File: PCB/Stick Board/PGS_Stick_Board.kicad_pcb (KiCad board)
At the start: 2 copper layers, 37.5 x 29.7 mm, 10 parts, among them J1 Molex 505110-0892, SW1 GL1807SYAE-002

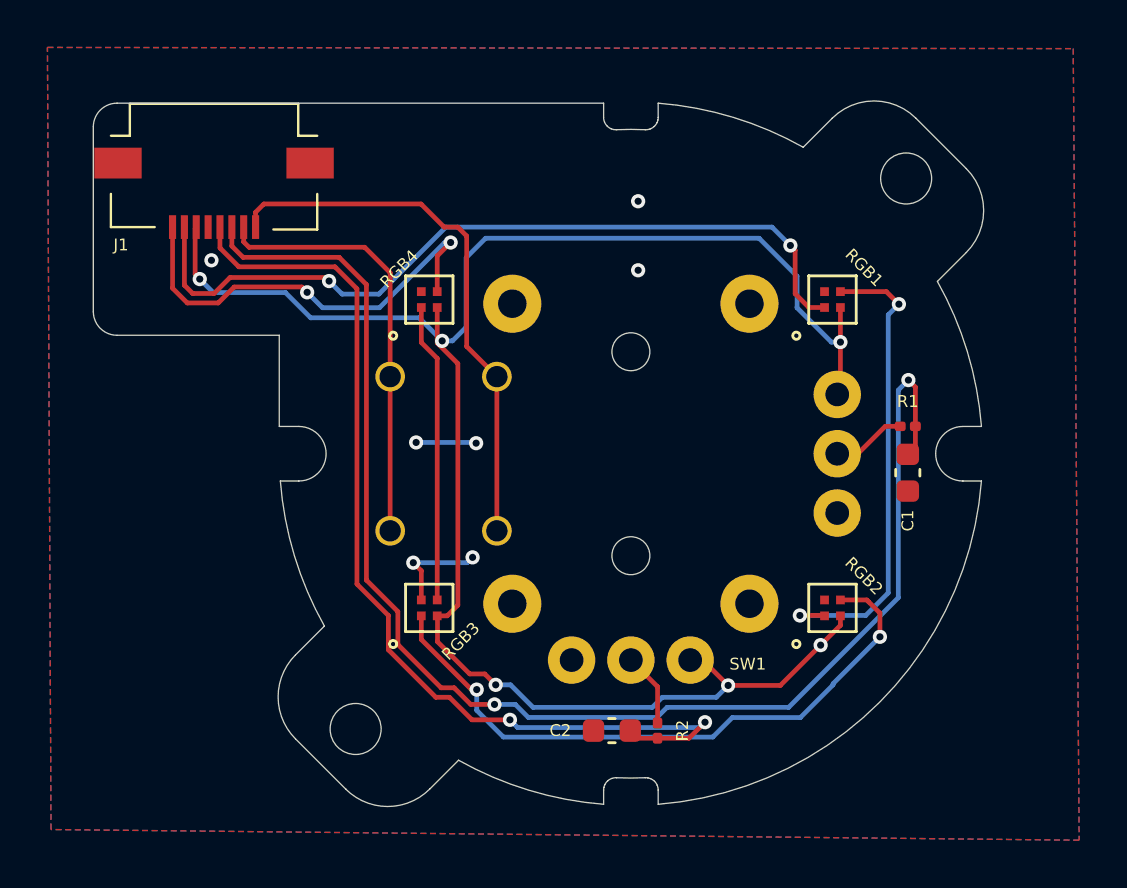
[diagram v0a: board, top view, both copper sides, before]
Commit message: Final Routing 3D Export
- Export 3D STEP models
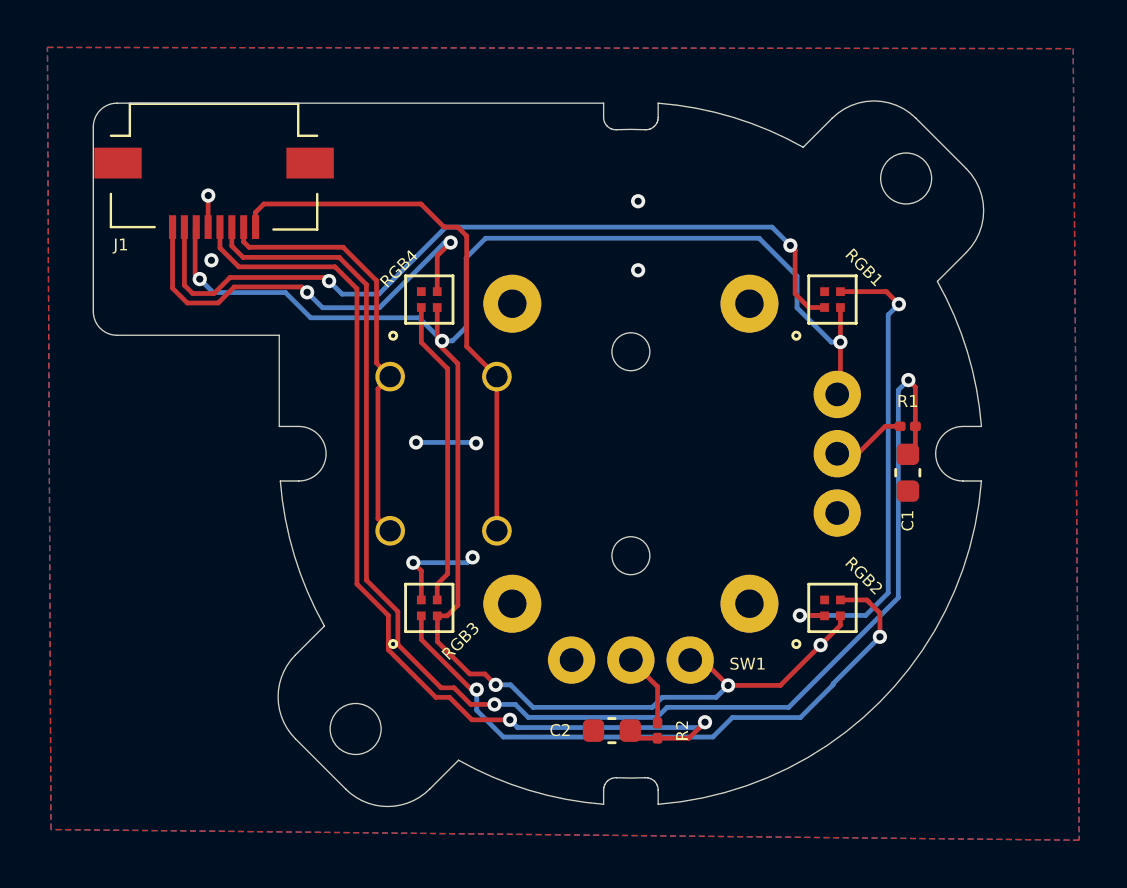
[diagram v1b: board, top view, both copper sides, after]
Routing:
- net GND: track 6.85 -> 8.18 mm, vias 7 -> 8
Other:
- board text added: "Designed by Mitch @ HHL"
- board text removed: "Designed By Mitch @ HHL"
